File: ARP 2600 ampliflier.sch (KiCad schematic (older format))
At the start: 32 parts, among them P1 CONN_01X04, P2 CONN_01X04, P3 CONN_01X04, P4 CONN_01X04, U1 TDA7269A, U2 LM7812CT, U3 LM7912CT

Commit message: routed
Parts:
- P1, P2, P3, P4: footprint Connectors_Terminal_Blocks:TerminalBlock_Pheonix_MPT-2.54mm_4pol -> w_conn_mpt:mpt_0,5%2f4-2,54
- U1: footprint w_to:Multiwatt11 -> MyModules:Multiwatt11-6400BG
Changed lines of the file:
@@
 F 0 "U1" H 3000 5900 50  0000 C CNN
 F 1 "TDA7269A" H 3525 4675 100 0000 C CNN
-F 2 "w_to:Multiwatt11" H 4500 5025 60  0001 C CNN
+F 2 "MyModules:Multiwatt11-6400BG" H 4500 5025 60  0001 C CNN
 F 3 "" H 4500 5025 60  0000 C CNN
 	1    3550 4675
@@
 F 0 "P3" H 6450 2925 50  0000 C CNN
 F 1 "CONN_01X04" V 6550 2675 50  0000 C CNN
-F 2 "Connectors_Terminal_Blocks:TerminalBlock_Pheonix_MPT-2.54mm_4pol" H 6450 2675 60  0001 C CNN
+F 2 "w_conn_mpt:mpt_0,5%2f4-2,54" H 6450 2675 60  0001 C CNN
 F 3 "" H 6450 2675 60  0000 C CNN
 	1    6450 2675
@@
 F 0 "P1" H 1675 4650 50  0000 C CNN
 F 1 "CONN_01X04" V 1775 4400 50  0000 C CNN
-F 2 "Connectors_Terminal_Blocks:TerminalBlock_Pheonix_MPT-2.54mm_4pol" H 1675 4400 60  0001 C CNN
+F 2 "w_conn_mpt:mpt_0,5%2f4-2,54" H 1675 4400 60  0001 C CNN
 F 3 "" H 1675 4400 60  0000 C CNN
 	1    1675 4400
@@
 F 0 "P2" H 6250 4925 50  0000 C CNN
 F 1 "CONN_01X04" V 6350 4675 50  0000 C CNN
-F 2 "Connectors_Terminal_Blocks:TerminalBlock_Pheonix_MPT-2.54mm_4pol" H 6250 4675 60  0001 C CNN
+F 2 "w_conn_mpt:mpt_0,5%2f4-2,54" H 6250 4675 60  0001 C CNN
 F 3 "" H 6250 4675 60  0000 C CNN
 	1    6250 4675
@@
 F 0 "P4" H 10625 2925 50  0000 C CNN
 F 1 "CONN_01X04" V 10725 2675 50  0000 C CNN
-F 2 "Connectors_Terminal_Blocks:TerminalBlock_Pheonix_MPT-2.54mm_4pol" H 10625 2675 60  0001 C CNN
+F 2 "w_conn_mpt:mpt_0,5%2f4-2,54" H 10625 2675 60  0001 C CNN
 F 3 "" H 10625 2675 60  0000 C CNN
 	1    10625 2675

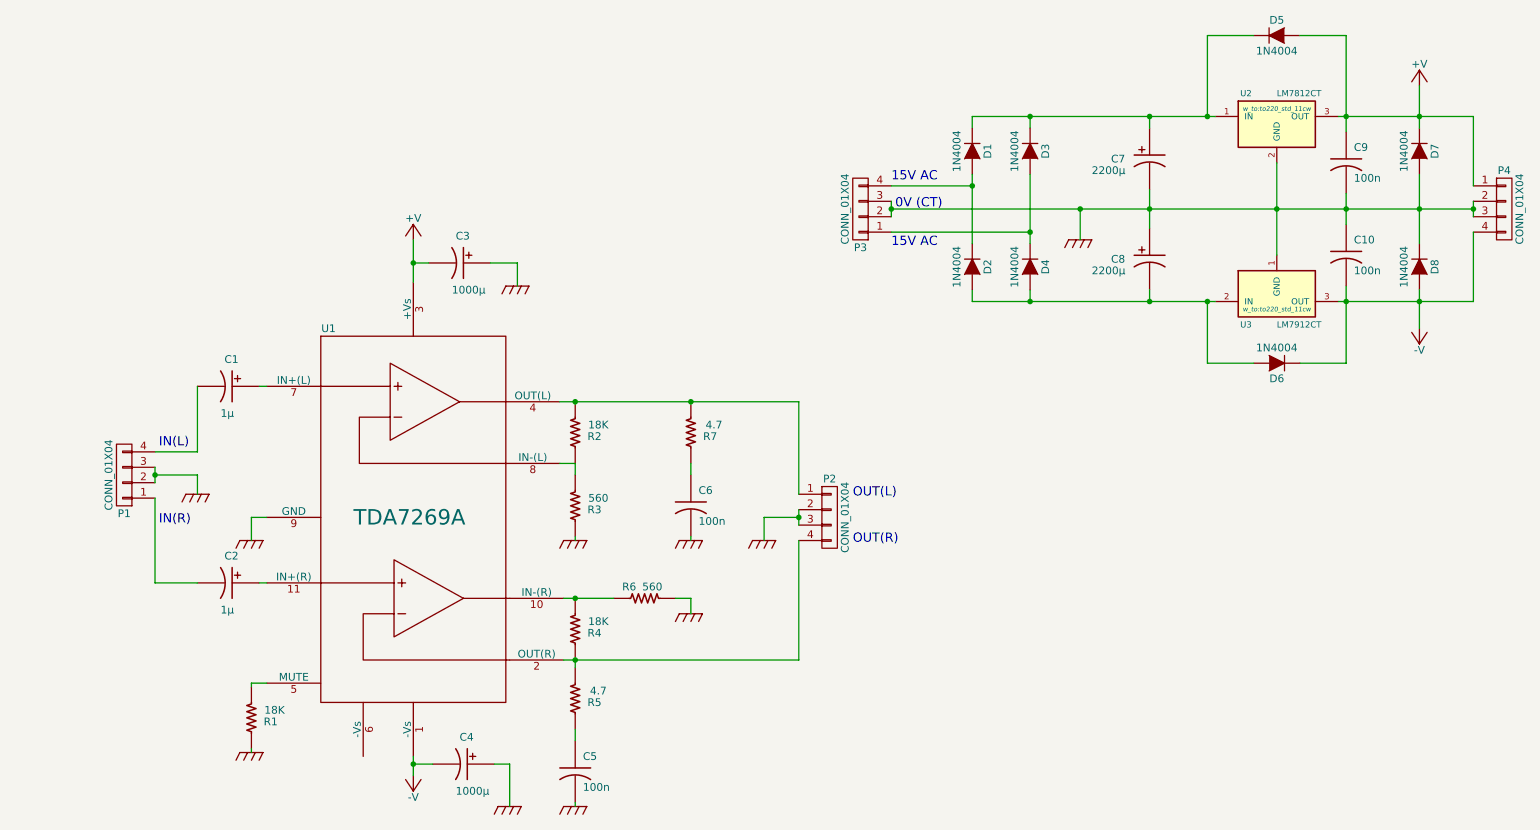
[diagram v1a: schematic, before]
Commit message: added standby/mute control during power up, generated gerbers
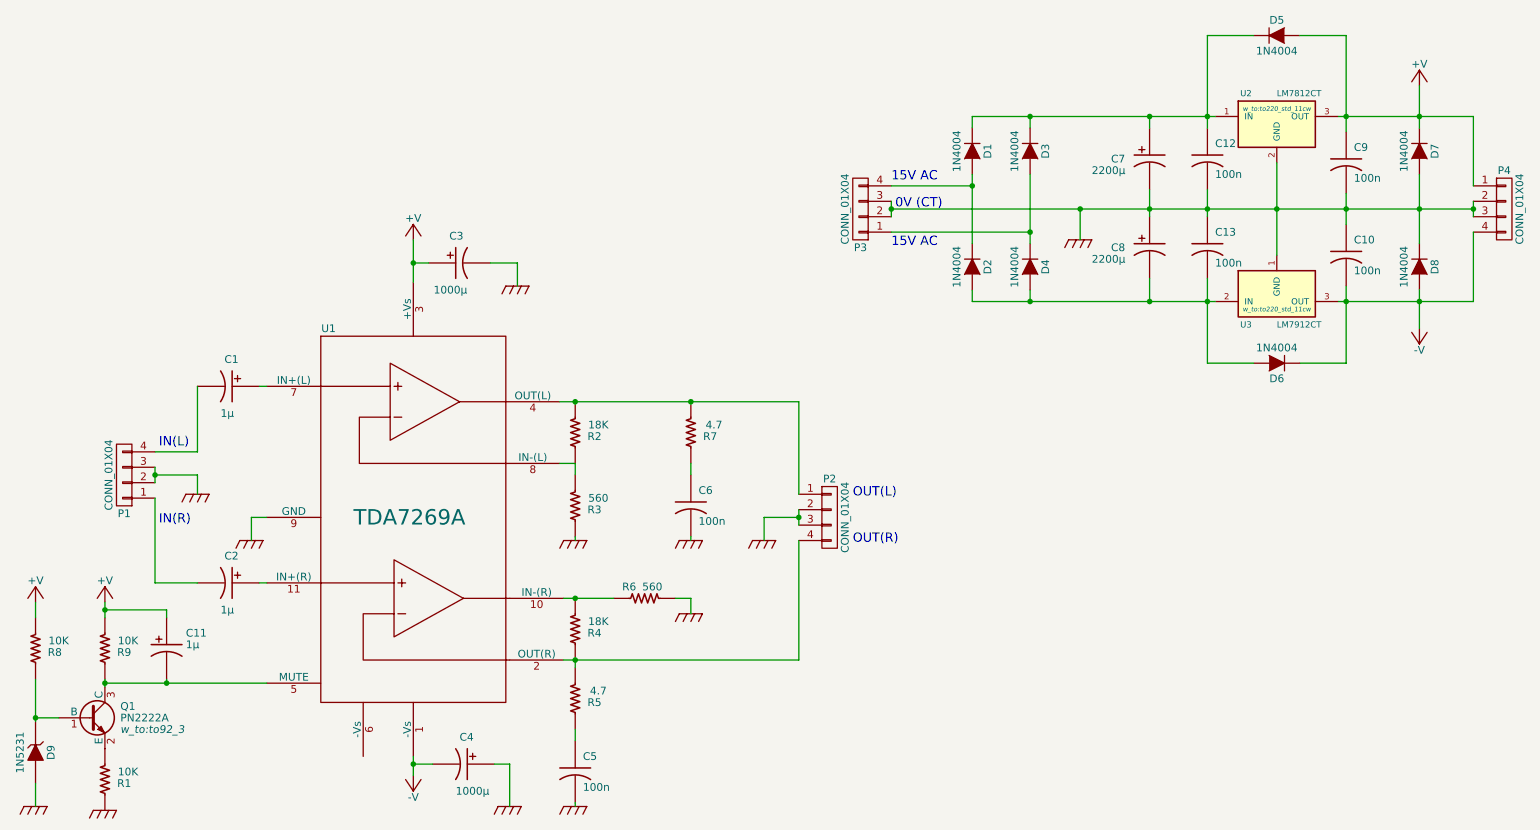
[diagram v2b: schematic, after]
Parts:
- added C11: 1µ, MyModules:2MM-POL-CAP, symbol CP_US
- added C12, C13: 100n, Capacitors_THT:C_Disc_D6_P5, symbol C_US
- added D9: 1N5231, Diodes_THT:Diode_DO-35_SOD27_Horizontal_RM10, symbol ZENER
- added Q1: PN2222A, w_to:to92_3, symbol PN2222A
- added R8, R9: 10K, Resistors_THT:Resistor_Horizontal_RM10mm, symbol R_US
- R1: value 18K -> 10K
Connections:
- net +V: now also C3.1 (+), C11.1 (+), R8.1, R9.1; no longer C3.2 (-)
- net GND: now also C3.2 (-), C12.2, C13.1, D9.2 (A); no longer C3.1 (+)
- net at U1.5 (MUTE): now also C11.2 (-), Q1.3 (C), R9.2; no longer R1.1
- net at C7.1 (+), D1.1 (K), D3.1 (K)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: now also C12.1
- net at C8.2 (-), D2.2 (A), D4.2 (A)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: now also C13.2
- new net: Q1.2 (E), R1.1
- new net: D9.1 (K), Q1.1 (B), R8.2
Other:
- moved on the sheet: C8, R1

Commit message: ready to order
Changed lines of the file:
@@
 	2600 5100 2550 5100
 $Comp
-L R_GND #PWR6
+L R_GND #PWR01
 U 1 1 5850DE34
 P 2500 4825
-F 0 "#PWR6" H 2500 4825 30  0001 C CNN
+F 0 "#PWR01" H 2500 4825 30  0001 C CNN
 F 1 "R_GND" H 2500 4725 30  0001 C CNN
 F 2 "" H 2500 4825 60  0000 C CNN
@@
 	2500 4675 2500 4825
 $Comp
-L +V #PWR7
+L +V #PWR02
 U 1 1 5850DEC0
 P 3550 2875
-F 0 "#PWR7" H 3550 2725 50  0001 C CNN
+F 0 "#PWR02" H 3550 2725 50  0001 C CNN
 F 1 "+V" H 3550 3015 50  0000 C CNN
 F 2 "" H 3550 2875 60  0000 C CNN
@@
 $EndComp
 $Comp
-L -V #PWR8
+L -V #PWR03
 U 1 1 5850DF28
 P 3550 6350
-F 0 "#PWR8" H 3550 6200 50  0001 C CNN
+F 0 "#PWR03" H 3550 6200 50  0001 C CNN
 F 1 "-V" H 3550 6490 50  0000 C CNN
 F 2 "" H 3550 6350 60  0000 C CNN
@@
 $EndComp
 $Comp
-L R_GND #PWR11
+L R_GND #PWR04
 U 1 1 5850E496
 P 4600 4825
-F 0 "#PWR11" H 4600 4825 30  0001 C CNN
+F 0 "#PWR04" H 4600 4825 30  0001 C CNN
 F 1 "R_GND" H 4600 4725 30  0001 C CNN
 F 2 "" H 4600 4825 60  0000 C CNN
@@
 $EndComp
 Wire Wire Line
-	4500 3925 4600 3925
-Wire Wire Line
-	4600 3925 5350 3925
-Wire Wire Line
-	5350 3925 6050 3925
+	4500 3925 6050 3925
 Wire Wire Line
 	4500 4325 4600 4325
@@
 	4600 4325 4600 4400
 Wire Wire Line
-	4525 5200 4600 5200
-Wire Wire Line
-	4600 5200 4850 5200
-Wire Wire Line
-	4525 5600 4600 5600
-Wire Wire Line
-	4600 5600 6050 5600
+	4525 5200 4850 5200
+Wire Wire Line
+	4525 5600 6050 5600
 Wire Wire Line
 	4600 4800 4600 4825
@@
 $EndComp
 $Comp
-L R_GND #PWR4
+L R_GND #PWR05
 U 1 1 5850EAED
 P 1550 6575
-F 0 "#PWR4" H 1550 6575 30  0001 C CNN
+F 0 "#PWR05" H 1550 6575 30  0001 C CNN
 F 1 "R_GND" H 1550 6475 30  0001 C CNN
 F 2 "" H 1550 6575 60  0000 C CNN
@@
 $EndComp
 Wire Wire Line
-	1550 5750 1950 5750
-Wire Wire Line
-	1950 5750 2600 5750
+	1550 5750 2600 5750
 $Comp
 L CP_US C4
@@
 $EndComp
 Wire Wire Line
-	3550 6225 3550 6275
-Wire Wire Line
-	3550 6275 3550 6350
+	3550 6225 3550 6350
 Wire Wire Line
 	3675 6275 3550 6275
@@
 	5350 4325 5350 4400
 $Comp
-L R_GND #PWR13
+L R_GND #PWR06
 U 1 1 5850F339
 P 5350 4825
-F 0 "#PWR13" H 5350 4825 30  0001 C CNN
+F 0 "#PWR06" H 5350 4825 30  0001 C CNN
 F 1 "R_GND" H 5350 4725 30  0001 C CNN
 F 2 "" H 5350 4825 60  0000 C CNN
@@
 Connection ~ 4600 5200
 $Comp
-L R_GND #PWR14
+L R_GND #PWR07
 U 1 1 5850F569
 P 5350 5300
-F 0 "#PWR14" H 5350 5300 30  0001 C CNN
+F 0 "#PWR07" H 5350 5300 30  0001 C CNN
 F 1 "R_GND" H 5350 5200 30  0001 C CNN
 F 2 "" H 5350 5300 60  0000 C CNN
@@
 	4600 6050 4600 6125
 $Comp
-L R_GND #PWR12
+L R_GND #PWR08
 U 1 1 5850F671
 P 4600 6550
-F 0 "#PWR12" H 4600 6550 30  0001 C CNN
+F 0 "#PWR08" H 4600 6550 30  0001 C CNN
 F 1 "R_GND" H 4600 6450 30  0001 C CNN
 F 2 "" H 4600 6550 60  0000 C CNN
@@
 Connection ~ 4600 5600
 $Comp
-L R_GND #PWR9
+L R_GND #PWR09
 U 1 1 5850FB09
 P 4175 6550
-F 0 "#PWR9" H 4175 6550 30  0001 C CNN
+F 0 "#PWR09" H 4175 6550 30  0001 C CNN
 F 1 "R_GND" H 4175 6450 30  0001 C CNN
 F 2 "" H 4175 6550 60  0000 C CNN
@@
 $EndComp
 $Comp
-L R_GND #PWR10
+L R_GND #PWR010
 U 1 1 5850FCE4
 P 4225 3175
-F 0 "#PWR10" H 4225 3175 30  0001 C CNN
+F 0 "#PWR010" H 4225 3175 30  0001 C CNN
 F 1 "R_GND" H 4225 3075 30  0001 C CNN
 F 2 "" H 4225 3175 60  0000 C CNN
@@
 	4225 3025 4225 3175
 Wire Wire Line
-	3550 2875 3550 3025
-Wire Wire Line
-	3550 3025 3550 3150
+	3550 2875 3550 3150
 Wire Wire Line
 	3650 3025 3550 3025
@@
 	9000 1550 8700 1550
 Wire Wire Line
-	8700 1550 8700 2075
-Wire Wire Line
-	8700 2075 8700 2150
-Wire Wire Line
-	7175 2075 7550 2075
-Wire Wire Line
-	7550 2075 8325 2075
-Wire Wire Line
-	8325 2075 8700 2075
-Wire Wire Line
-	8700 2075 8750 2075
+	8700 1550 8700 2150
+Wire Wire Line
+	7175 2075 8750 2075
 Wire Wire Line
 	9300 1550 9600 1550
 Wire Wire Line
-	9600 1550 9600 2075
-Wire Wire Line
-	9600 2075 9600 2175
-Wire Wire Line
-	9550 2075 9600 2075
-Wire Wire Line
-	9600 2075 10075 2075
-Wire Wire Line
-	10075 2075 10425 2075
-$Comp
-L R_GND #PWR16
+	9600 1550 9600 2175
+Wire Wire Line
+	9550 2075 10425 2075
+$Comp
+L R_GND #PWR011
 U 1 1 58511EF5
 P 7875 2875
-F 0 "#PWR16" H 7875 2875 30  0001 C CNN
+F 0 "#PWR011" H 7875 2875 30  0001 C CNN
 F 1 "R_GND" H 7875 2775 30  0001 C CNN
 F 2 "" H 7875 2875 60  0000 C CNN
@@
 $EndComp
 Wire Wire Line
-	8325 2550 8325 2675
-Wire Wire Line
-	8325 2675 8325 2725
-Wire Wire Line
-	6650 2675 7875 2675
-Wire Wire Line
-	7875 2675 8325 2675
-Wire Wire Line
-	8325 2675 8700 2675
-Wire Wire Line
-	8700 2675 9150 2675
-Wire Wire Line
-	9150 2675 9600 2675
-Wire Wire Line
-	9600 2675 10075 2675
-Wire Wire Line
-	10075 2675 10425 2675
+	8325 2550 8325 2725
+Wire Wire Line
+	6650 2675 10425 2675
 Connection ~ 8325 2675
 Wire Wire Line
-	9150 2375 9150 2675
-Wire Wire Line
-	9150 2675 9150 2975
+	9150 2375 9150 2975
 Connection ~ 9150 2675
 Wire Wire Line
 	8325 3275 8325 3125
 Wire Wire Line
-	7175 3275 7550 3275
-Wire Wire Line
-	7550 3275 8325 3275
-Wire Wire Line
-	8325 3275 8700 3275
-Wire Wire Line
-	8700 3275 8750 3275
+	7175 3275 8750 3275
 $Comp
 L D D6
@@
 	9600 3675 9300 3675
 Wire Wire Line
-	9600 3175 9600 3275
-Wire Wire Line
-	9600 3275 9600 3675
-Wire Wire Line
-	9550 3275 9600 3275
-Wire Wire Line
-	9600 3275 10075 3275
-Wire Wire Line
-	10075 3275 10425 3275
+	9600 3175 9600 3675
+Wire Wire Line
+	9550 3275 10425 3275
 Wire Wire Line
 	8700 3675 9000 3675
 Wire Wire Line
-	8700 3125 8700 3275
-Wire Wire Line
-	8700 3275 8700 3675
+	8700 3125 8700 3675
 Connection ~ 8700 3275
 Wire Wire Line
-	7550 2450 7550 2825
-Wire Wire Line
-	7550 2825 7550 2900
+	7550 2450 7550 2900
 Wire Wire Line
 	7550 3275 7550 3200
@@
 $EndComp
 Wire Wire Line
-	6650 2625 6650 2675
-Wire Wire Line
-	6650 2675 6650 2725
+	6650 2625 6650 2725
 Connection ~ 6650 2675
 Wire Wire Line
@@
 Connection ~ 7550 2825
 Wire Wire Line
-	7175 2450 7175 2525
-Wire Wire Line
-	7175 2525 7175 2900
+	7175 2450 7175 2900
 Wire Wire Line
 	6650 2525 7175 2525
@@
 	1875 5100 2150 5100
 Wire Wire Line
-	1875 4350 1875 4400
-Wire Wire Line
-	1875 4400 1875 4450
-$Comp
-L R_GND #PWR5
+	1875 4350 1875 4450
+$Comp
+L R_GND #PWR012
 U 1 1 58514121
 P 2150 4525
-F 0 "#PWR5" H 2150 4525 30  0001 C CNN
+F 0 "#PWR012" H 2150 4525 30  0001 C CNN
 F 1 "R_GND" H 2150 4425 30  0001 C CNN
 F 2 "" H 2150 4525 60  0000 C CNN
@@
 	6050 5600 6050 4825
 Wire Wire Line
-	6050 4625 6050 4675
-Wire Wire Line
-	6050 4675 6050 4725
-$Comp
-L R_GND #PWR15
+	6050 4625 6050 4725
+$Comp
+L R_GND #PWR013
 U 1 1 58514655
 P 5825 4825
-F 0 "#PWR15" H 5825 4825 30  0001 C CNN
+F 0 "#PWR013" H 5825 4825 30  0001 C CNN
 F 1 "R_GND" H 5825 4725 30  0001 C CNN
 F 2 "" H 5825 4825 60  0000 C CNN
@@
 Connection ~ 9600 3275
 Wire Wire Line
-	9600 2575 9600 2675
-Wire Wire Line
-	9600 2675 9600 2775
+	9600 2575 9600 2775
 $Comp
 L D D7
@@
 $EndComp
 Wire Wire Line
-	10075 2450 10075 2675
-Wire Wire Line
-	10075 2675 10075 2900
+	10075 2450 10075 2900
 Connection ~ 9600 2675
 Connection ~ 10075 2675
 Wire Wire Line
-	10075 3200 10075 3275
-Wire Wire Line
-	10075 3275 10075 3450
-$Comp
-L +V #PWR17
+	10075 3200 10075 3450
+$Comp
+L +V #PWR014
 U 1 1 585155F6
 P 10075 1875
-F 0 "#PWR17" H 10075 1725 50  0001 C CNN
+F 0 "#PWR014" H 10075 1725 50  0001 C CNN
 F 1 "+V" H 10075 2015 50  0000 C CNN
 F 2 "" H 10075 1875 60  0000 C CNN
@@
 $EndComp
 Wire Wire Line
-	10075 1875 10075 2075
-Wire Wire Line
-	10075 2075 10075 2150
+	10075 1875 10075 2150
 Connection ~ 10075 2075
 $Comp
-L -V #PWR18
+L -V #PWR015
 U 1 1 58515DB0
 P 10075 3450
-F 0 "#PWR18" H 10075 3300 50  0001 C CNN
+F 0 "#PWR015" H 10075 3300 50  0001 C CNN
 F 1 "-V" H 10075 3590 50  0000 C CNN
 F 2 "" H 10075 3450 60  0000 C CNN
@@
 	10425 3275 10425 2825
 Wire Wire Line
-	10425 2625 10425 2675
-Wire Wire Line
-	10425 2675 10425 2725
+	10425 2625 10425 2725
 Connection ~ 10425 2675
 Text Notes 1900 4225 0    60   ~ 0
@@
 $EndComp
 $Comp
-L R_GND #PWR2
+L R_GND #PWR016
 U 1 1 5855B56F
 P 1100 6550
-F 0 "#PWR2" H 1100 6550 30  0001 C CNN
+F 0 "#PWR016" H 1100 6550 30  0001 C CNN
 F 1 "R_GND" H 1100 6450 30  0001 C CNN
 F 2 "" H 1100 6550 60  0000 C CNN
@@
 	1100 6550 1100 6400
 Wire Wire Line
-	1550 5725 1550 5750
-Wire Wire Line
-	1550 5750 1550 5775
+	1550 5725 1550 5775
 Wire Wire Line
 	1250 5975 1100 5975
 Wire Wire Line
-	1100 5725 1100 5975
-Wire Wire Line
-	1100 5975 1100 6000
+	1100 5725 1100 6000
 $Comp
 L R_US R8
@@
 Connection ~ 1100 5975
 $Comp
-L +V #PWR1
+L +V #PWR017
 U 1 1 5855C37A
 P 1100 5225
-F 0 "#PWR1" H 1100 5075 50  0001 C CNN
+F 0 "#PWR017" H 1100 5075 50  0001 C CNN
 F 1 "+V" H 1100 5365 50  0000 C CNN
 F 2 "" H 1100 5225 60  0000 C CNN
@@
 	1950 5275 1550 5275
 Wire Wire Line
-	1550 5225 1550 5275
-Wire Wire Line
-	1550 5275 1550 5325
-$Comp
-L +V #PWR3
+	1550 5225 1550 5325
+$Comp
+L +V #PWR018
 U 1 1 5855CD17
 P 1550 5225
-F 0 "#PWR3" H 1550 5075 50  0001 C CNN
+F 0 "#PWR018" H 1550 5075 50  0001 C CNN
 F 1 "+V" H 1550 5365 50  0000 C CNN
 F 2 "" H 1550 5225 60  0000 C CNN
@@
 $EndComp
 Wire Wire Line
-	8700 2550 8700 2675
-Wire Wire Line
-	8700 2675 8700 2725
+	8700 2550 8700 2725
 Connection ~ 8700 2675
 $EndSCHEMATC
